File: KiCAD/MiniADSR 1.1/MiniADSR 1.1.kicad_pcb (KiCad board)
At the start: 2 copper layers, 105 x 128.5 mm, 50 parts, among them J1 INPUT, J2 OUTPUT, J3 JST_BUS, J4 ControlBoard_Pins, J5 IDC_BUS, J6 MainBoard_Pins, Q1 BC547, Q2 BC547, Q3 BC547, U1 LM555, U2 TL072

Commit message: Added fixes after fist build
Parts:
- C2: value *10uF -> 1uF
- C3: value 100uF -> 2.2uF
- D1, D2, D3, D4, D5: value 4148 -> 1N4148
- POT_SUSTAIN1: value 1M -> 10k
- Q1, Q2, Q3: footprint Package_TO_SOT_THT:TO-92_Inline_Wide -> Package_TO_SOT_THT:TO-92_Inline
- U1: value LM555 -> LM555xN
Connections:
- R7 pad 1: +12V -> Net-(C1-Pad2)
- U1 pad 4: +12V -> Net-(C1-Pad2)
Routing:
- net Net-(C1-Pad2): track 45.5 -> 53.9 mm
- net Net-(Q2-Pad2): track 15.4 -> 19.7 mm
- net Net-(R8-Pad1): track 29.7 -> 28.6 mm
- net +12V: track 129.6 -> 130.5 mm
- net Net-(Q3-Pad2): track 9.76 -> 9.00 mm
- net Net-(D1-Pad1): track 25.8 -> 26.5 mm
- net Net-(Q1-Pad1): track 10.4 -> 10.9 mm
- net GND2: vias 68 -> 65

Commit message: Added version number
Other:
- board text added: "MiniADSR v1.1"

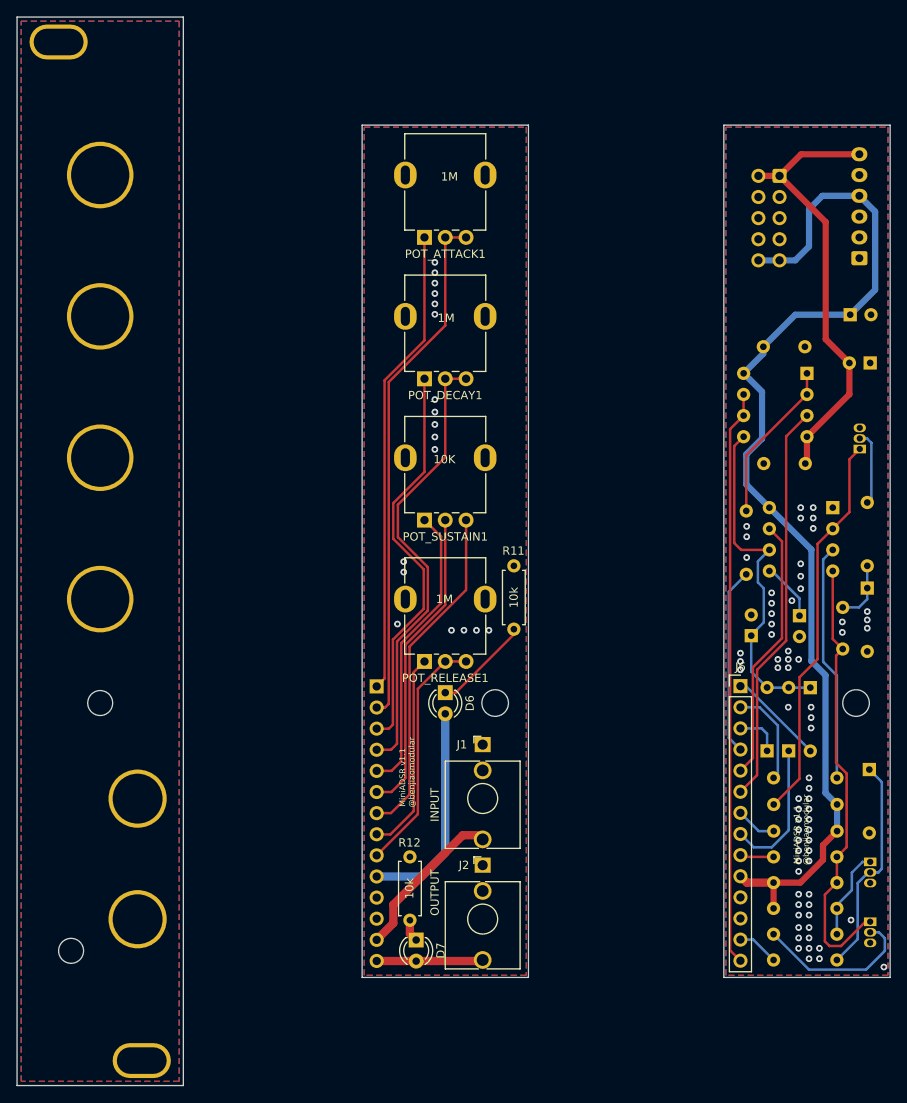
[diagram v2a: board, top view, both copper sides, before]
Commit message: Redesigned PCB layout, added cap for longer decay
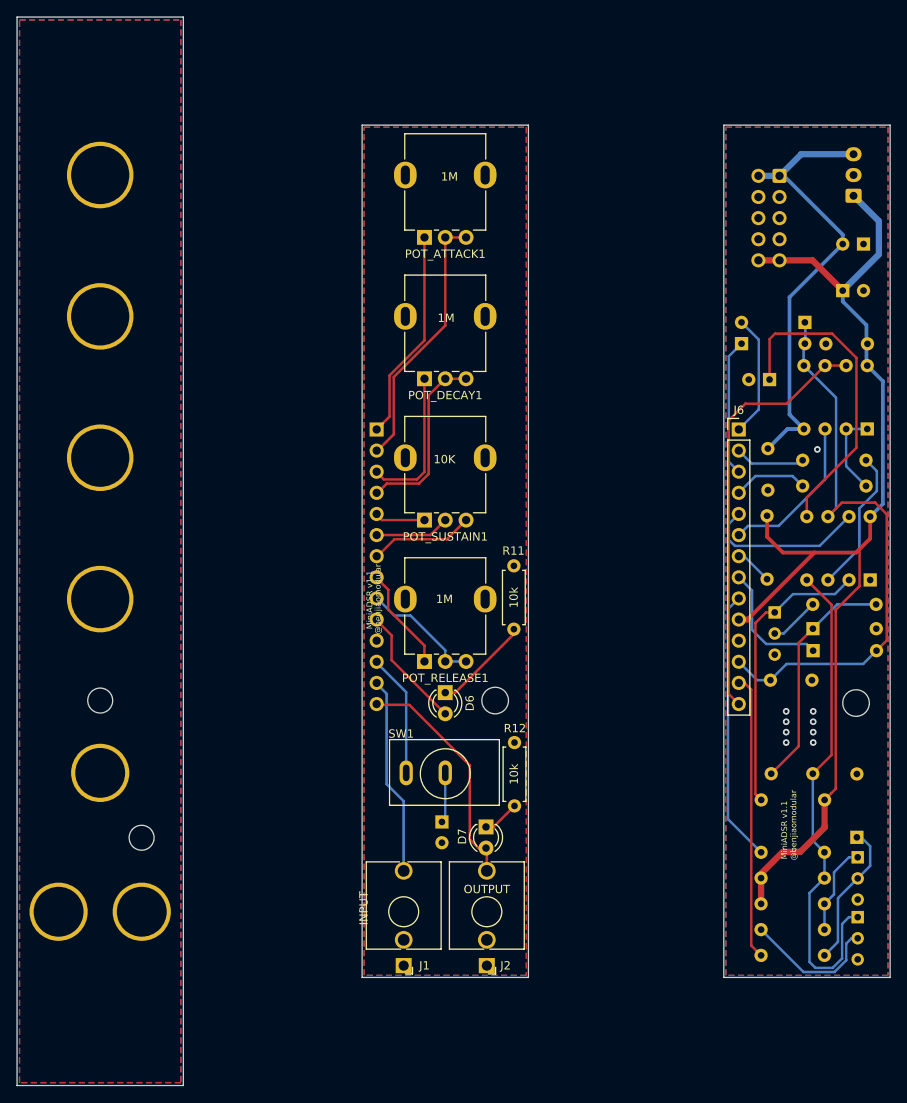
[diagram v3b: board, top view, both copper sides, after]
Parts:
- removed the REF** at (50.0, 40.0)
- added C8: 470nF, benjiaomodular:Capacitor_Rect_L7.2mm_W2.5mm_P5.00mm, B.Cu at (145.6, 119.8)
- added REF**: PanelHole_ToggleSwitch_MTS-101, benjiaomodular:PanelHole_ToggleSwitch_MTS-101, F.Cu at (60.0, 130.9)
- added SW1: SW_DIP_x01, benjiaomodular:ToggleSwitch_MTS-101_SPST, F.Cu at (101.5, 131.0)
- C2: value 1uF -> 10uF
- C3: value 2.2uF -> 4.7uF*
- J3: footprint Connector_JST:JST_XH_B6B-XH-A_1x06_P2.50mm_Vertical -> Connector_JST:JST_XH_B3B-XH-A_1x03_P2.50mm_Vertical
- Q1, Q2, Q3: footprint Package_TO_SOT_THT:TO-92_Inline -> Package_TO_SOT_THT:TO-92_Inline_Wide
- REF**: moved to B.Cu
- moved D5 49.1 mm to (137.1, 79.3), turned to 0 degrees
- moved D4 43.9 mm to (144.8, 76.7), turned to 180 degrees
- moved C3 43.4 mm to (101.1, 136.8), turned to 270 degrees
- moved R8 38.4 mm to (152.1, 93.3)
- moved J4 30.9 mm to (93.2, 89.6)
- moved J6 30.9 mm to (136.8, 89.6)
- moved R9 30.3 mm to (140.2, 107.6), turned to 90 degrees
- moved C2 28.6 mm to (140.5, 83.6), turned to 180 degrees
- moved REF** 28.2 mm to (55.0, 154.1), turned to 180 degrees
- moved J1 28.2 mm to (96.5, 154.1), turned to 180 degrees
- moved Q3 22.2 mm to (141.1, 111.6), turned to 270 degrees
- moved C1 21.8 mm to (140.7, 131.0), turned to 0 degrees
- moved R12 18.6 mm to (109.8, 127.2)
- moved D7 16.0 mm to (106.4, 137.4)
- moved R10 14.7 mm to (152.1, 96.4), turned to 180 degrees
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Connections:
- C3 pad 2: GND2 -> GND1
- D3 pad 2: Net-(C3-Pad1) -> B12
- D4 pad 1: Net-(C3-Pad1) -> B12
- D5 pad 2: Net-(C3-Pad1) -> B12
- J3 pad 1: (no net) -> +12V
- J3 pad 2: (no net) -> GND2
- J3 pad 3: (no net) -> -12V
- J4 pad 12: GND1 -> A12
- J6 pad 12: GND2 -> B12
- U1 pad 6: Net-(C3-Pad1) -> B12
- U2 pad 5: Net-(C3-Pad1) -> B12
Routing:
- net B12: track 0.00 -> 69.7 mm
- net Net-(C3-Pad1): track 41.9 -> 6.07 mm
- net A6: track 54.5 -> 22.0 mm
- net A4: track 63.0 -> 31.7 mm
- net Net-(C2-Pad1): track 7.07 -> 38.4 mm
- net A3: track 56.4 -> 25.5 mm
- net A5: track 48.3 -> 17.7 mm
- net B8: track 48.6 -> 19.2 mm
- net B1: track 4.99 -> 34.3 mm
- net A7: track 35.2 -> 6.02 mm
- net B11: track 4.07 -> 32.7 mm
- net A8: track 37.2 -> 9.04 mm
- net A9: track 40.7 -> 12.6 mm
- net Net-(C1-Pad1): track 7.36 -> 28.3 mm
- net B2: track 69.3 -> 51.5 mm
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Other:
- outline, holes or cut-outs redrawn
- board text added: "(+)"
- board text added: "LONG"
- board text added: "SHORT"
- board text added: "to 4.7uF"
